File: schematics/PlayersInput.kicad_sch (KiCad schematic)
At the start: 28 parts

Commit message: WIP
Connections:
- net 1P=01 is gone; now on net 1P-01: IBF.2 (IN)
- net 1P=02 is gone; now on net 1P-02: IBF.2 (IN)
- net 1P=03 is gone; now on net 1P-03: IBF.2 (IN)
- net 2P=01 is gone; now on net 2P-01: IBF.2 (IN)
- net 2P=02 is gone; now on net 2P-02: IBF.2 (IN)
- net 2P=03 is gone; now on net 2P-03: IBF.2 (IN)
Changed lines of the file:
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@@
     )
   )
-  (global_label "2P=01" (shape input) (at 121.92 223.52 0) (fields_autoplaced)
+  (global_label "2P-01" (shape input) (at 121.92 223.52 0) (fields_autoplaced)
     (effects (font (size 1.27 1.27)) (justify left))
     (property "Intersheetrefs" "${INTERSHEET_REFS}" (at 131.3761 223.52 0)
@@
     )
   )
-  (global_label "1P=03" (shape input) (at 121.92 209.55 0) (fields_autoplaced)
+  (global_label "1P-03" (shape input) (at 121.92 209.55 0) (fields_autoplaced)
     (effects (font (size 1.27 1.27)) (justify left))
     (property "Intersheetrefs" "${INTERSHEET_REFS}" (at 131.3761 209.55 0)
@@
     )
   )
-  (global_label "1P=02" (shape input) (at 121.92 195.58 0) (fields_autoplaced)
+  (global_label "1P-02" (shape input) (at 121.92 195.58 0) (fields_autoplaced)
     (effects (font (size 1.27 1.27)) (justify left))
     (property "Intersheetrefs" "${INTERSHEET_REFS}" (at 131.3761 195.58 0)
@@
     )
   )
-  (global_label "2P=03" (shape input) (at 121.92 251.46 0) (fields_autoplaced)
+  (global_label "2P-03" (shape input) (at 121.92 251.46 0) (fields_autoplaced)
     (effects (font (size 1.27 1.27)) (justify left))
     (property "Intersheetrefs" "${INTERSHEET_REFS}" (at 131.3761 251.46 0)
@@
     )
   )
-  (global_label "2P=02" (shape input) (at 121.92 237.49 0) (fields_autoplaced)
+  (global_label "2P-02" (shape input) (at 121.92 237.49 0) (fields_autoplaced)
     (effects (font (size 1.27 1.27)) (justify left))
     (property "Intersheetrefs" "${INTERSHEET_REFS}" (at 131.3761 237.49 0)
@@
     )
   )
-  (global_label "1P=01" (shape input) (at 121.92 181.61 0) (fields_autoplaced)
+  (global_label "1P-01" (shape input) (at 121.92 181.61 0) (fields_autoplaced)
     (effects (font (size 1.27 1.27)) (justify left))
     (property "Intersheetrefs" "${INTERSHEET_REFS}" (at 131.3761 181.61 0)

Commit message: update "main" schematics
Adding LSPC2-A2, NEO-B1, L0 ROM
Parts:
- NEO-C1: footprint (none) -> Package_QFP:PQFP-100_14x20mm_P0.65mm; symbol 0-Custom-Frater_Library:NEO-C1 -> 0-Custom-SNK:NEO-C1
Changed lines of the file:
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@@
     )
   )
-  (symbol (lib_id "0-Custom-Frater_Library:NEO-C1") (at 81.28 101.6 0) (unit 1)
+  (symbol (lib_id "0-Custom-SNK:NEO-C1") (at 81.28 101.6 0) (unit 1)
     (in_bom yes) (on_board yes) (dnp no)
     (property "Reference" "NEO-C1" (at 66.04 20.32 0)
@@
       (effects (font (size 1.27 1.27)))
     )
-    (property "Footprint" "" (at 81.28 81.28 0)
+    (property "Footprint" "Package_QFP:PQFP-100_14x20mm_P0.65mm" (at 81.28 81.28 0)
       (effects (font (size 1.27 1.27)) hide)
     )
-    (property "Datasheet" "" (at 81.28 81.28 0)
+    (property "Datasheet" "https://wiki.neogeodev.org/index.php?title=NEO-C1" (at 81.28 81.28 0)
       (effects (font (size 1.27 1.27)) hide)
     )

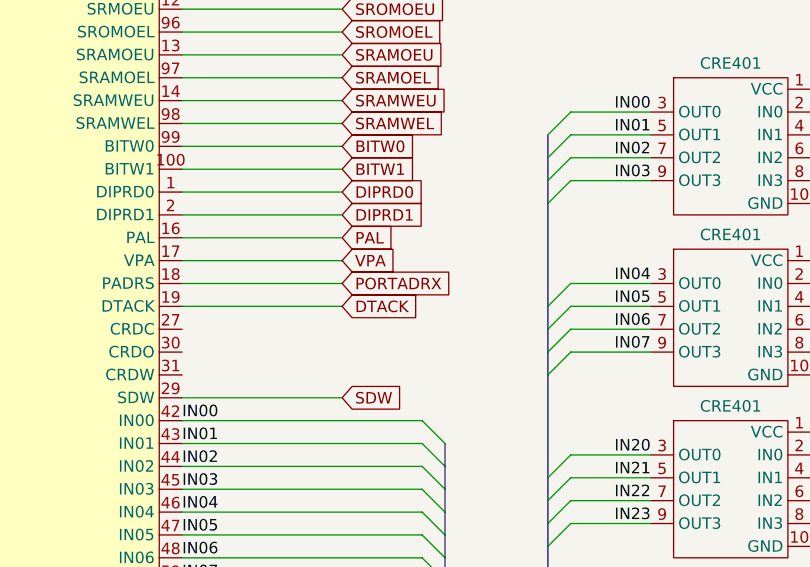
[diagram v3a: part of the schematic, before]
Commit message: Complete Page 2 (LSPC2-A2)
Complete "Main" page LSPC2, NEO-IO, NEO-B1, NEO-ZMC2 & SFix Rom LO Rom
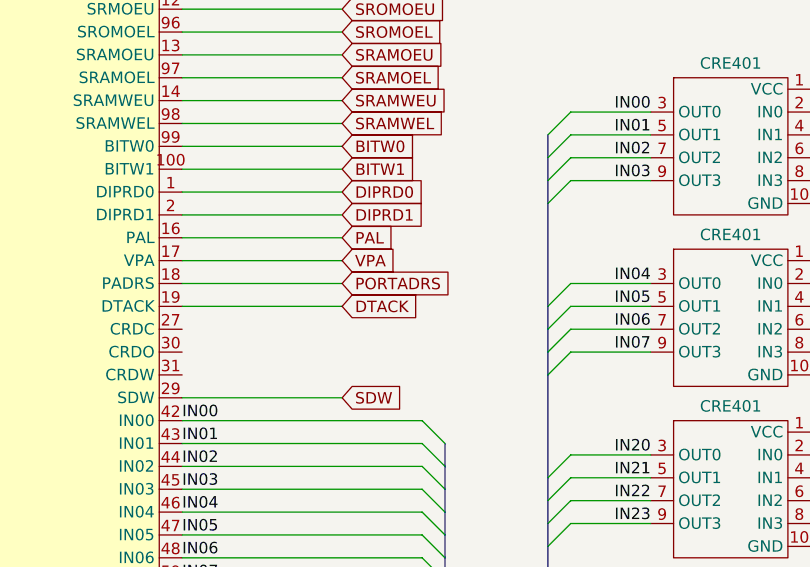
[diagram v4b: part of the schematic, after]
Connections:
- net PORTADRX renamed PORTADRS
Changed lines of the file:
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@@
     )
   )
-  (global_label "PORTADRX" (shape input) (at 118.11 85.09 0) (fields_autoplaced)
+  (global_label "PORTADRS" (shape input) (at 118.11 85.09 0) (fields_autoplaced)
     (effects (font (size 1.27 1.27)) (justify left))
     (property "Intersheetrefs" "${INTERSHEET_REFS}" (at 130.7714 85.09 0)

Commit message: Complete pages 1-4
completion of pages 1 to 4
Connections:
- net SOO0 renamed SOD0
- net SOO1 renamed SOD1
- net SOO2 renamed SOD2
- net SOO3 renamed SOD3
- net SOO4 renamed SOD4
- net SOO5 renamed SOD5
- net SOO6 renamed SOD6
- net SOO7 renamed SOD7

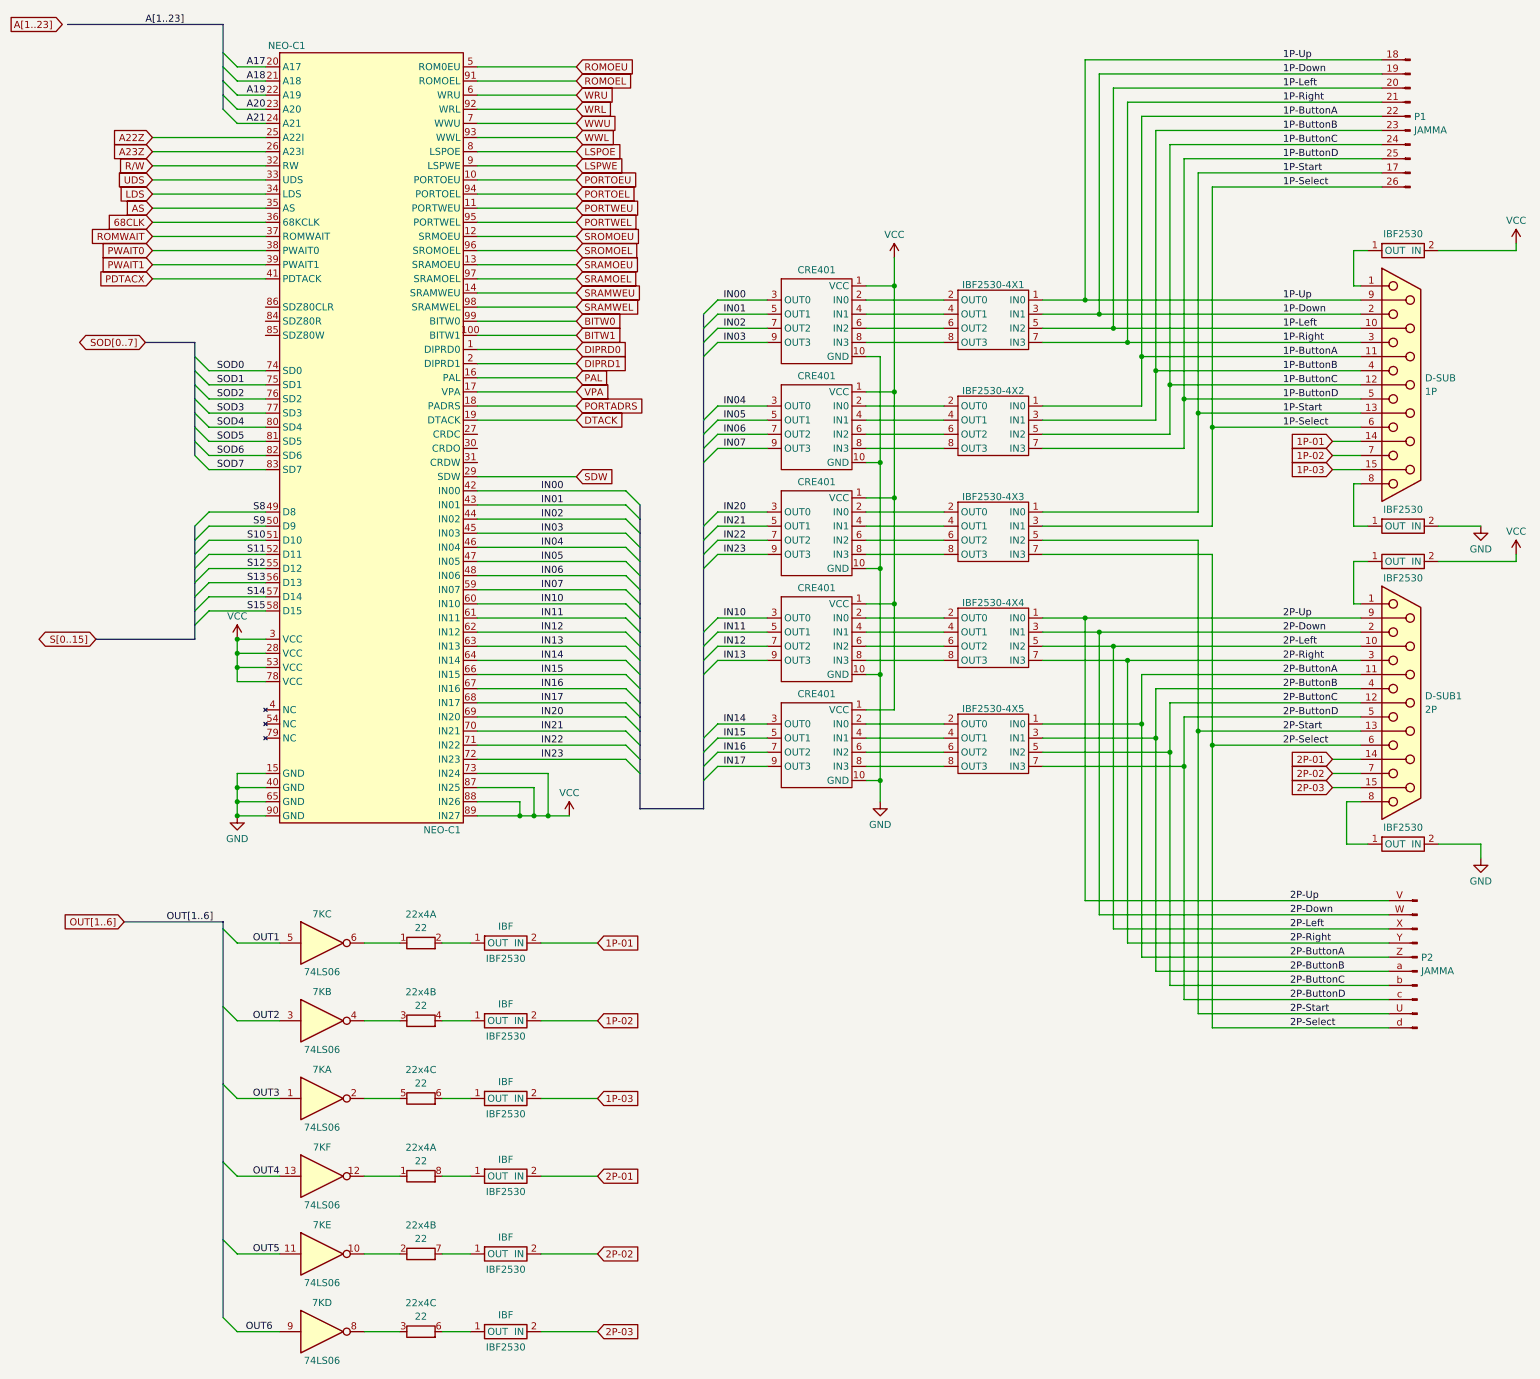
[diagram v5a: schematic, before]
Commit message: Audio Amp + player's button LED & marquee + Coins Up + 45% raiser card connectors
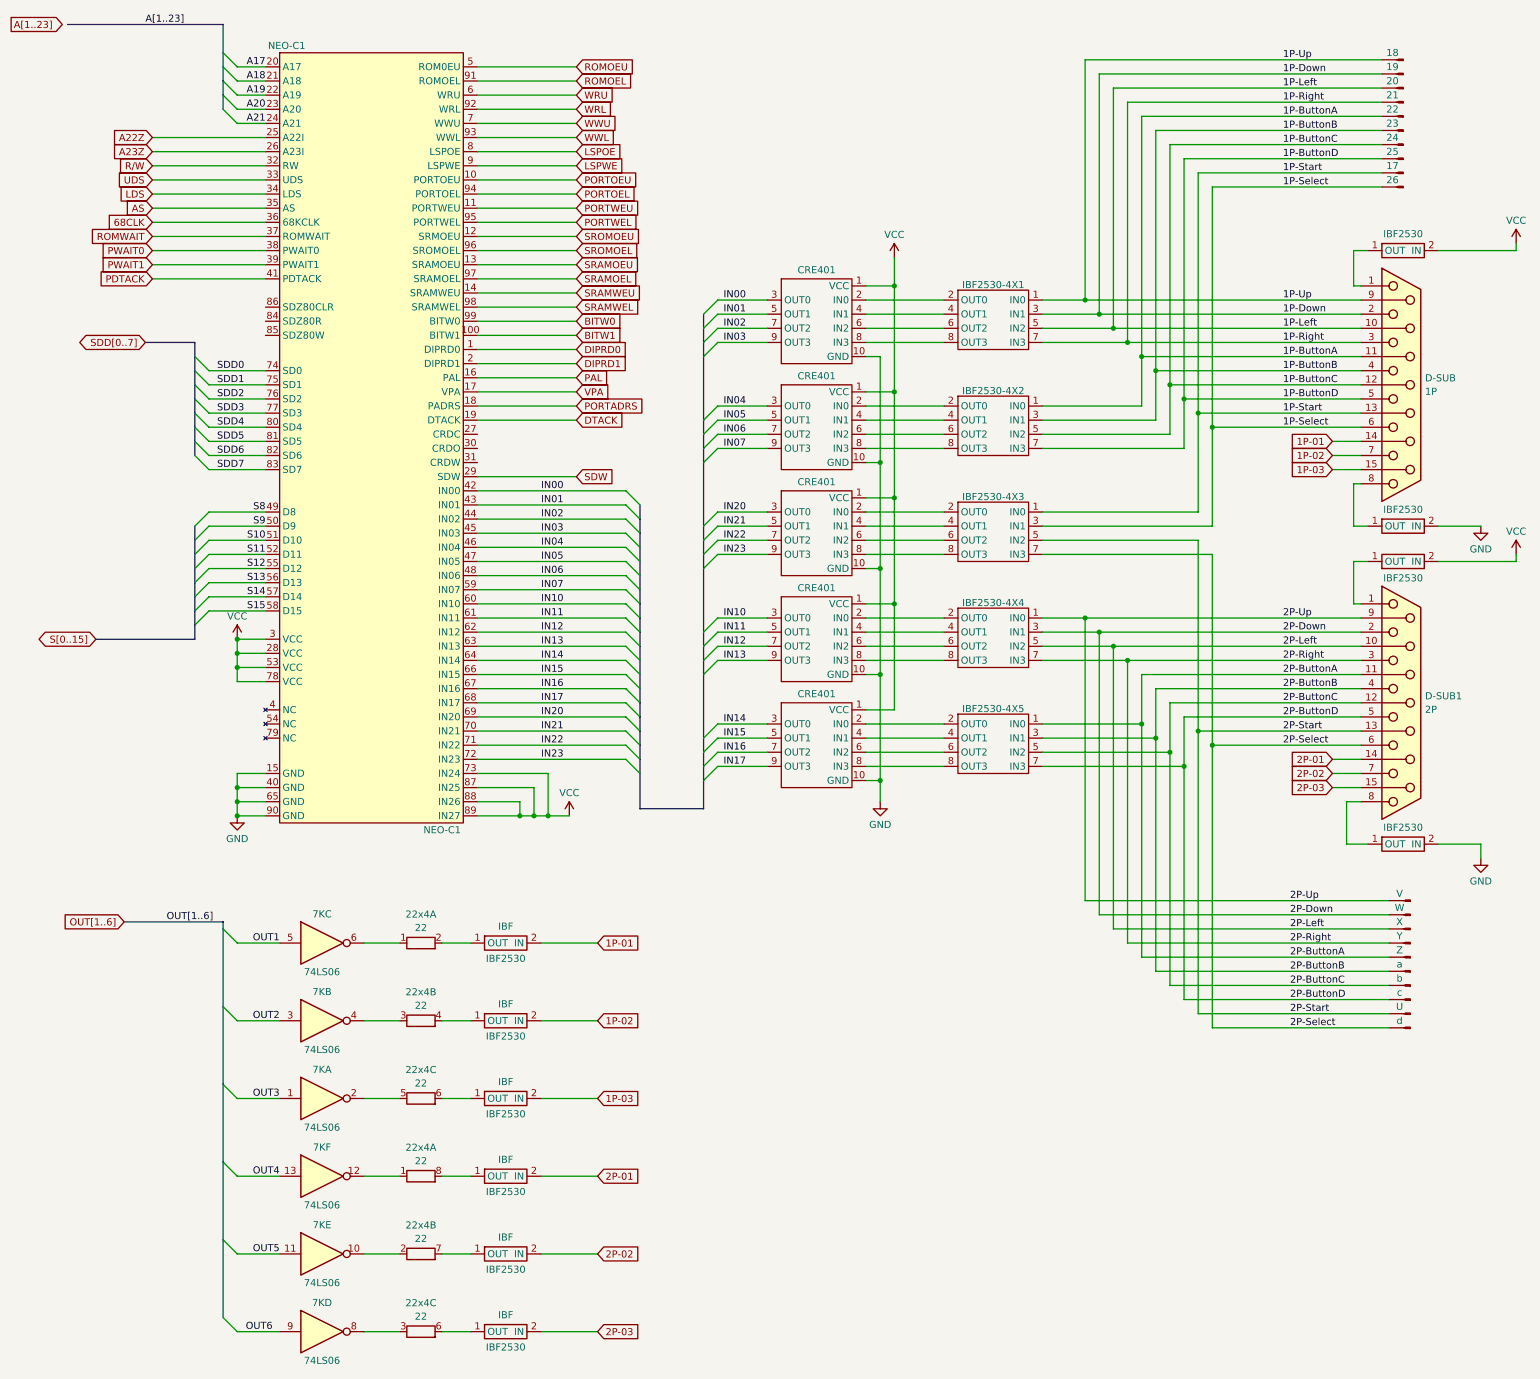
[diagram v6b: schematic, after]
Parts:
- removed JAMMA: P2, symbol Connector:Conn_01x10_Pin
- removed JAMMA: P1, symbol Connector:Conn_01x10_Pin
- added JAMMA1, JAMMA31, JAMMA32, JAMMA33, JAMMA34, JAMMA35, JAMMA36, JAMMA37, JAMMA38, JAMMA39, JAMMA40, JAMMA41, JAMMA42, JAMMA43, JAMMA44, JAMMA45, JAMMA46, JAMMA47, JAMMA48, JAMMA49: ~, symbol 0-Custom-SNK:JAMMA_PAD
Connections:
- net 1P-ButtonA: now also JAMMA35.6
- net 1P-ButtonB: now also JAMMA36.6
- net 1P-ButtonC: now also JAMMA37.6
- net 1P-ButtonD: now also JAMMA38.6
- net 1P-Down: now also JAMMA32.6
- net 1P-Left: now also JAMMA33.6
- net 1P-Right: now also JAMMA34.6
- net 1P-Select: now also JAMMA40.6
- net 1P-Start: now also JAMMA39.6
- net 1P-Up: now also JAMMA31.6
- net 2P-ButtonA: now also JAMMA44.6
- net 2P-ButtonB: now also JAMMA45.6
- net 2P-ButtonC: now also JAMMA46.6
- net 2P-ButtonD: now also JAMMA47.6
- net 2P-Down: now also JAMMA41.6
- net 2P-Left: now also JAMMA42.6
- net 2P-Right: now also JAMMA43.6
- net 2P-Select: now also JAMMA49.6
- net 2P-Start: now also JAMMA48.6
- net 2P-Up: now also JAMMA1.6
- net PDTACX renamed PDTACK
- net SOD0 renamed SDD0
- net SOD1 renamed SDD1
- net SOD2 renamed SDD2
- net SOD3 renamed SDD3
- net SOD4 renamed SDD4
- net SOD5 renamed SDD5
- net SOD6 renamed SDD6
- net SOD7 renamed SDD7

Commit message: typos
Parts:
- 7K: footprint (none) -> Package_DIP:DIP-14_W7.62mm
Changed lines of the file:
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@@
     (comment 3 "Converted by Frater ")
     (comment 4 "NEO-GEO MVS MV1F")
+    (comment 9 "https://github.com/Neo-Geo-Hardwares/Schematics-MV1F")
   )
   (junction (at 214.63 128.27) (diameter 0) (color 0 0 0 0)
@@
       (effects (font (size 1.27 1.27)))
     )
-    (property "Footprint" "" (at 72.39 251.46 0)
+    (property "Footprint" "Package_DIP:DIP-14_W7.62mm" (at 72.39 251.46 0)
       (effects (font (size 1.27 1.27)) hide)
     )
@@
       (effects (font (size 1.27 1.27)))
     )
-    (property "Footprint" "" (at 72.39 195.58 0)
+    (property "Footprint" "Package_DIP:DIP-14_W7.62mm" (at 72.39 195.58 0)
       (effects (font (size 1.27 1.27)) hide)
     )
@@
       (effects (font (size 1.27 1.27)))
     )
-    (property "Footprint" "" (at 72.39 223.52 0)
+    (property "Footprint" "Package_DIP:DIP-14_W7.62mm" (at 72.39 223.52 0)
       (effects (font (size 1.27 1.27)) hide)
     )
@@
       (effects (font (size 1.27 1.27)))
     )
-    (property "Footprint" "" (at 72.39 181.61 0)
+    (property "Footprint" "Package_DIP:DIP-14_W7.62mm" (at 72.39 181.61 0)
       (effects (font (size 1.27 1.27)) hide)
     )
@@
       (effects (font (size 1.27 1.27)))
     )
-    (property "Footprint" "" (at 72.39 209.55 0)
+    (property "Footprint" "Package_DIP:DIP-14_W7.62mm" (at 72.39 209.55 0)
       (effects (font (size 1.27 1.27)) hide)
     )
@@
       (effects (font (size 1.27 1.27)))
     )
-    (property "Footprint" "" (at 72.39 237.49 0)
+    (property "Footprint" "Package_DIP:DIP-14_W7.62mm" (at 72.39 237.49 0)
       (effects (font (size 1.27 1.27)) hide)
     )
